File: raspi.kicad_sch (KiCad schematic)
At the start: 56 parts, among them J8 Conn_01x03, J9 debug_probe, SW1 SW_Omron_B3FS, U6 RP2350B-QFN80, U8 16Mbit PSRAM, X1 ASE-xxxMHz

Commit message: Finnished pinouts
pending input from firmware
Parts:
- added TP32, TP33, TP34: Spare, symbol Connector:TestPoint
- X1: value ASE-xxxMHz -> ASE-12.000MHZ-L-C-T
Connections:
- net BAR_CS: now also U6.26 (GPIO25)
- net Encoder0_A: now also U6.18 (GPIO18)
- net Encoder0_B: now also U6.19 (GPIO19)
- net Encoder1_A: now also U6.3 (GPIO6)
- net Encoder1_B: now also U6.4 (GPIO7)
- net Expansion_RX: now also R26.1; no longer R27.2
- net Expansion_TX: now also R27.2; no longer R26.1
- net GPS_INT: now also U6.9 (GPIO11)
- net GPS_PPS: now also U6.6 (GPIO8)
- net GPS_RESET: now also U6.7 (GPIO9)
- net GPS_RX: now also U6.1 (GPIO4)
- net GPS_SAFE: now also U6.8 (GPIO10)
- net GPS_TX: now also U6.2 (GPIO5)
- net IMU_CLK: now also U6.42 (GPIO33)
- net IMU_CS: now also U6.27 (GPIO26)
- net IMU_INT: now also U6.43 (GPIO34)
- net SD_CS: now also U6.25 (GPIO24)
- net SD_DET: now also U6.40 (GPIO32)
- net Spare_CS_0: now also U6.28 (GPIO27)
- net Spare_CS_1: now also U6.36 (GPIO28)
- net Spare_CS_2: now also U6.37 (GPIO29)
- net at U6.11 (GPIO12): now also TP32.1
- net at U6.12 (GPIO13): now also TP33.1
- net at U6.13 (GPIO14): now also TP34.1
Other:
- note added: "Note on UARTS: Prefix determines source of the TX. For example Raspi_TX indicates that the TX is coming from the Raspi"
- note added: "Resources RASPI_TX/RX | UART0 M1 | PWM1 GPS_TX/RX | UART1 M0 | PWM0 MCU_SPI | SPI0"

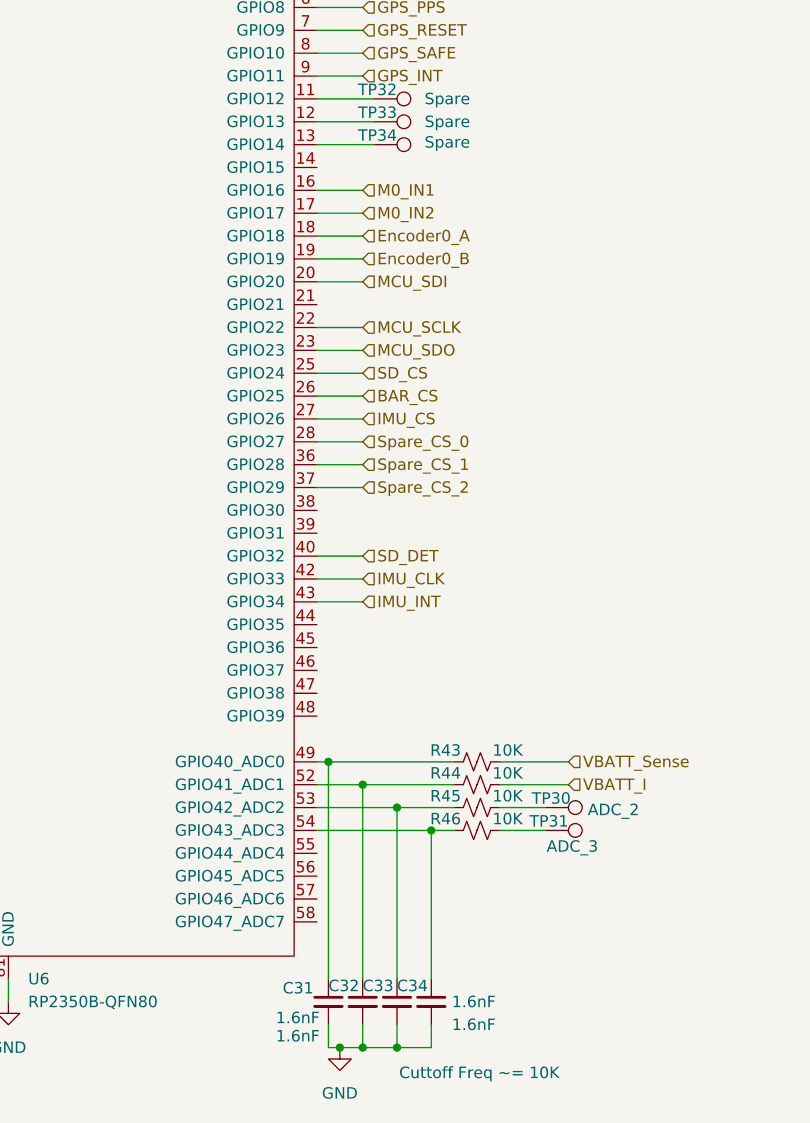
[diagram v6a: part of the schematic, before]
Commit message: Updated sheet to sheet pinout
Updated pinouts and cleared ERCs
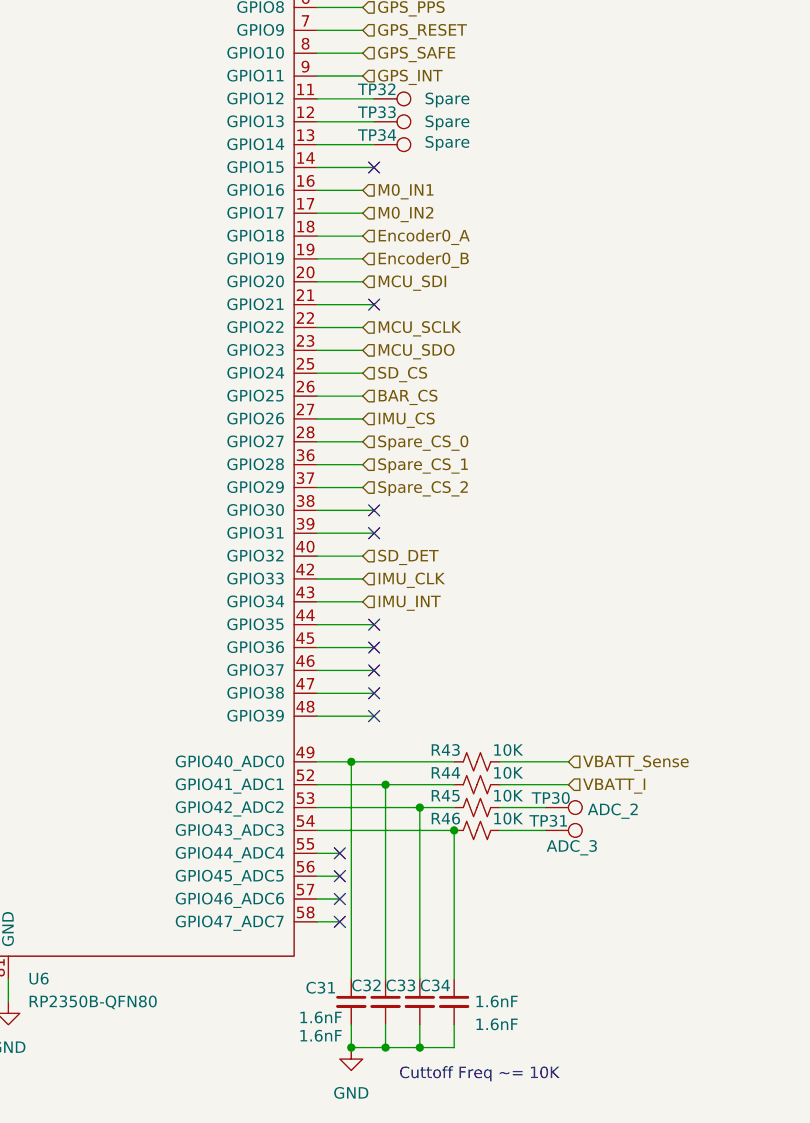
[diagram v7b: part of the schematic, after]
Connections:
- no-connect marks 1 -> 14
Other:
- moved on the sheet: C31, C32, C33, C34

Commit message: started layout
Preliminary footprint selection
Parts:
- C20, C21, C22, C27, C28, C29, C30, C31, C32, C33, C34, C35, C36, C37, C38, C39, C40, C41, C42, C43, C44: footprint (none) -> Capacitor_SMD:C_0603_1608Metric_Pad1.08x0.95mm_HandSolder
- C23, C24, C25, C26: footprint (none) -> Capacitor_SMD:C_0805_2012Metric_Pad1.18x1.45mm_HandSolder
- J8: footprint (none) -> Connector_PinHeader_2.54mm:PinHeader_1x03_P2.54mm_Vertical_SMD_Pin1Left
- J9: footprint (none) -> Connector_JST:JST_SH_SM03B-SRSS-TB_1x03-1MP_P1.00mm_Horizontal
- L2: footprint (none) -> Inductor_SMD:L_1008_2520Metric; PN (none) -> LQM2HPN3R3MG0L
- R24, R25, R26, R27, R32, R33, R34, R35, R36, R41, R43, R44, R45, R46, R47, R48, R49: footprint (none) -> Resistor_SMD:R_0603_1608Metric
- SW1: footprint (none) -> Button_Switch_SMD:SW_SPST_B3S-1000
- TP23, TP26, TP27, TP28, TP29, TP30, TP31, TP32, TP33, TP34: footprint (none) -> TestPoint:TestPoint_Pad_1.0x1.0mm
- U6: footprint (none) -> RP2350_KiCad-main:RP2350B_QFN-80_EP_10.573x10.573_Pitch0.4mm
- U8: footprint (none) -> Package_SO:SOIC-8-1EP_3.9x4.9mm_P1.27mm_EP2.29x3mm
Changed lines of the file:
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@@
 			)
 		)
-		(property "Footprint" ""
+		(property "Footprint" "Resistor_SMD:R_0603_1608Metric"
 			(at 60.96 36.83 0)
 			(effects
@@
 			)
 		)
-		(property "Footprint" ""
+		(property "Footprint" "Capacitor_SMD:C_0805_2012Metric_Pad1.18x1.45mm_HandSolder"
 			(at 64.77 58.42 0)
 			(effects
@@
 			)
 		)
-		(property "Footprint" ""
+		(property "Footprint" "Resistor_SMD:R_0603_1608Metric"
 			(at 157.48 44.45 0)
 			(effects
@@
 			)
 		)
-		(property "Footprint" ""
+		(property "Footprint" "TestPoint:TestPoint_Pad_1.0x1.0mm"
 			(at 170.18 168.91 0)
 			(effects
@@
 			)
 		)
-		(property "Footprint" ""
+		(property "Footprint" "TestPoint:TestPoint_Pad_1.0x1.0mm"
 			(at 151.13 95.25 0)
 			(effects
@@
 			)
 		)
-		(property "Footprint" ""
+		(property "Footprint" "Resistor_SMD:R_0603_1608Metric"
 			(at 30.48 148.59 0)
 			(effects
@@
 			)
 		)
-		(property "Footprint" ""
+		(property "Footprint" "Connector_PinHeader_2.54mm:PinHeader_1x03_P2.54mm_Vertical_SMD_Pin1Left"
 			(at 267.97 21.59 0)
 			(effects
@@
 			)
 		)
-		(property "Footprint" ""
+		(property "Footprint" "Connector_JST:JST_SH_SM03B-SRSS-TB_1x03-1MP_P1.00mm_Horizontal"
 			(at 20.32 146.05 0)
 			(effects
@@
 			)
 		)
-		(property "Footprint" ""
+		(property "Footprint" "TestPoint:TestPoint_Pad_1.0x1.0mm"
 			(at 170.18 171.45 0)
 			(effects
@@
 			)
 		)
-		(property "Footprint" ""
+		(property "Footprint" "Inductor_SMD:L_1008_2520Metric"
 			(at 69.85 55.88 0)
 			(effects
@@
 			)
 		)
+		(property "PN" "LQM2HPN3R3MG0L"
+			(at 69.85 55.88 90)
+			(effects
+				(font
+					(size 1.27 1.27)
+				)
+				(hide yes)
+			)
+		)
 		(pin "2"
 		)
@@
 			)
 		)
-		(property "Footprint" ""
+		(property "Footprint" "Resistor_SMD:R_0603_1608Metric"
 			(at 30.48 143.51 0)
 			(effects
@@
 			)
 		)
-		(property "Footprint" ""
+		(property "Footprint" "Capacitor_SMD:C_0603_1608Metric_Pad1.08x0.95mm_HandSolder"
 			(at 250.19 152.4 0)
 			(effects
@@
 			)
 		)
-		(property "Footprint" ""
+		(property "Footprint" "TestPoint:TestPoint_Pad_1.0x1.0mm"
 			(at 55.88 48.26 0)
 			(effects
@@
 			)
 		)
-		(property "Footprint" ""
+		(property "Footprint" "Button_Switch_SMD:SW_SPST_B3S-1000"
 			(at 264.16 142.24 0)
 			(effects
@@
 			)
 		)
-		(property "Footprint" ""
+		(property "Footprint" "Capacitor_SMD:C_0603_1608Metric_Pad1.08x0.95mm_HandSolder"
 			(at 33.02 187.96 0)
 			(effects
@@
 			)
 		)
-		(property "Footprint" ""
+		(property "Footprint" "TestPoint:TestPoint_Pad_1.0x1.0mm"
 			(at 151.13 90.17 0)
 			(effects
@@
 			)
 		)
-		(property "Footprint" ""
+		(property "Footprint" "Resistor_SMD:R_0603_1608Metric"
 			(at 162.56 163.83 0)
 			(effects
@@
 			)
 		)
-		(property "Footprint" ""
+		(property "Footprint" "Capacitor_SMD:C_0603_1608Metric_Pad1.08x0.95mm_HandSolder"
 			(at 147.32 50.8 0)
 			(effects
@@
 			)
 		)
-		(property "Footprint" ""
+		(property "Footprint" "Capacitor_SMD:C_0603_1608Metric_Pad1.08x0.95mm_HandSolder"
 			(at 26.67 187.96 0)
 			(effects
@@
 			)
 		)
-		(property "Footprint" ""
+		(property "Footprint" "Capacitor_SMD:C_0603_1608Metric_Pad1.08x0.95mm_HandSolder"
 			(at 152.4 185.42 0)
 			(effects
@@
 			)
 		)
-		(property "Footprint" ""
+		(property "Footprint" "Capacitor_SMD:C_0603_1608Metric_Pad1.08x0.95mm_HandSolder"
 			(at 54.61 187.96 0)
 			(effects
@@
 			)
 		)
-		(property "Footprint" ""
+		(property "Footprint" "Capacitor_SMD:C_0603_1608Metric_Pad1.08x0.95mm_HandSolder"
 			(at 148.59 185.42 0)
 			(effects
@@
 			)
 		)
-		(property "Footprint" ""
+		(property "Footprint" "TestPoint:TestPoint_Pad_1.0x1.0mm"
 			(at 165.1 49.53 0)
 			(effects
@@
 			)
 		)
-		(property "Footprint" ""
+		(property "Footprint" "Capacitor_SMD:C_0603_1608Metric_Pad1.08x0.95mm_HandSolder"
 			(at 69.85 187.96 0)
 			(effects
@@
 			)
 		)
-		(property "Footprint" ""
+		(property "Footprint" "Capacitor_SMD:C_0805_2012Metric_Pad1.18x1.45mm_HandSolder"
 			(at 67.31 22.86 0)
 			(effects
@@
 			)
 		)
-		(property "Footprint" ""
+		(property "Footprint" "Capacitor_SMD:C_0603_1608Metric_Pad1.08x0.95mm_HandSolder"
 			(at 39.37 187.96 0)
 			(effects
@@
 			)
 		)
-		(property "Footprint" ""
+		(property "Footprint" "Capacitor_SMD:C_0603_1608Metric_Pad1.08x0.95mm_HandSolder"
 			(at 62.23 187.96 0)
 			(effects
@@
 			)
 		)
-		(property "Footprint" ""
+		(property "Footprint" "Capacitor_SMD:C_0603_1608Metric_Pad1.08x0.95mm_HandSolder"
 			(at 46.99 187.96 0)
 			(effects
@@
 			)
 		)
-		(property "Footprint" ""
+		(property "Footprint" "Capacitor_SMD:C_0603_1608Metric_Pad1.08x0.95mm_HandSolder"
 			(at 133.35 25.4 0)
 			(effects
@@
 			)
 		)
-		(property "Footprint" ""
+		(property "Footprint" "Resistor_SMD:R_0603_1608Metric"
 			(at 21.59 101.6 0)
 			(effects
@@
 			)
 		)
-		(property "Footprint" ""
+		(property "Footprint" "Capacitor_SMD:C_0603_1608Metric_Pad1.08x0.95mm_HandSolder"
 			(at 77.47 187.96 0)
 			(effects
@@
 			)
 		)
-		(property "Footprint" ""
+		(property "Footprint" "Capacitor_SMD:C_0603_1608Metric_Pad1.08x0.95mm_HandSolder"
 			(at 74.93 22.86 0)
 			(effects
@@
 			)
 		)
-		(property "Footprint" ""
+		(property "Footprint" "Resistor_SMD:R_0603_1608Metric"
 			(at 243.84 19.05 0)
 			(effects
@@
 			)
 		)
-		(property "Footprint" ""
+		(property "Footprint" "Capacitor_SMD:C_0603_1608Metric_Pad1.08x0.95mm_HandSolder"
 			(at 156.21 185.42 0)
 			(effects
@@
 			)
 		)
-		(property "Footprint" ""
+		(property "Footprint" "Capacitor_SMD:C_0805_2012Metric_Pad1.18x1.45mm_HandSolder"
 			(at 66.04 40.64 0)
 			(effects
@@
 			)
 		)
-		(property "Footprint" ""
+		(property "Footprint" "Resistor_SMD:R_0603_1608Metric"
 			(at 162.56 161.29 0)
 			(effects
@@
 			)
 		)
-		(property "Footprint" ""
+		(property "Footprint" "Capacitor_SMD:C_0603_1608Metric_Pad1.08x0.95mm_HandSolder"
 			(at 152.4 50.8 0)
 			(effects
@@
 			)
 		)
-		(property "Footprint" ""
+		(property "Footprint" "Resistor_SMD:R_0603_1608Metric"
 			(at 139.7 21.59 0)
 			(effects
@@
 			)
 		)
-		(property "Footprint" ""
+		(property "Footprint" "TestPoint:TestPoint_Pad_1.0x1.0mm"
 			(at 165.1 52.07 0)
 			(effects
@@
 			)
 		)
-		(property "Footprint" ""
+		(property "Footprint" "Resistor_SMD:R_0603_1608Metric"
 			(at 162.56 166.37 0)
 			(effects
@@
 			)
 		)
-		(property "Footprint" ""
+		(property "Footprint" "Resistor_SMD:R_0603_1608Metric"
 			(at 243.84 21.59 0)
 			(effects
@@
 			)
 		)
-		(property "Footprint" ""
+		(property "Footprint" "Resistor_SMD:R_0603_1608Metric"
 			(at 157.48 46.99 0)
 			(effects
@@
 			)
 		)
-		(property "Footprint" ""
+		(property "Footprint" "Capacitor_SMD:C_0603_1608Metric_Pad1.08x0.95mm_HandSolder"
 			(at 20.32 187.96 0)
 			(effects
@@
 			)
 		)
-		(property "Footprint" ""
+		(property "Footprint" "Capacitor_SMD:C_0603_1608Metric_Pad1.08x0.95mm_HandSolder"
 			(at 81.28 22.86 0)
 			(effects
@@
 			)
 		)
-		(property "Footprint" ""
+		(property "Footprint" "Resistor_SMD:R_0603_1608Metric"
 			(at 250.19 143.51 0)
 			(effects
@@
 			)
 		)
-		(property "Footprint" ""
+		(property "Footprint" "RP2350_KiCad-main:RP2350B_QFN-80_EP_10.573x10.573_Pitch0.4mm"
 			(at 104.14 59.69 0)
 			(effects
@@
 			)
 		)
-		(property "Footprint" ""
+		(property "Footprint" "Package_SO:SOIC-8-1EP_3.9x4.9mm_P1.27mm_EP2.29x3mm"
 			(at 38.1 73.66 0)
 			(effects
@@
 			)
 		)
-		(property "Footprint" ""
+		(property "Footprint" "TestPoint:TestPoint_Pad_1.0x1.0mm"
 			(at 60.96 88.9 0)
 			(effects
@@
 			)
 		)
-		(property "Footprint" ""
+		(property "Footprint" "Capacitor_SMD:C_0603_1608Metric_Pad1.08x0.95mm_HandSolder"
 			(at 160.02 185.42 0)
 			(effects
@@
 			)
 		)
-		(property "Footprint" ""
+		(property "Footprint" "TestPoint:TestPoint_Pad_1.0x1.0mm"
 			(at 151.13 92.71 0)
 			(effects
@@
 			)
 		)
-		(property "Footprint" ""
+		(property "Footprint" "TestPoint:TestPoint_Pad_1.0x1.0mm"
 			(at 237.49 149.86 0)
 			(effects
@@
 			)
 		)
-		(property "Footprint" ""
+		(property "Footprint" "Resistor_SMD:R_0603_1608Metric"
 			(at 243.84 35.56 0)
 			(effects
@@
 			)
 		)
-		(property "Footprint" ""
+		(property "Footprint" "Capacitor_SMD:C_0603_1608Metric_Pad1.08x0.95mm_HandSolder"
 			(at 38.1 93.98 0)
 			(effects
@@
 			)
 		)
-		(property "Footprint" ""
+		(property "Footprint" "Capacitor_SMD:C_0603_1608Metric_Pad1.08x0.95mm_HandSolder"
 			(at 22.86 71.12 0)
 			(effects
@@
 			)
 		)
-		(property "Footprint" ""
+		(property "Footprint" "Resistor_SMD:R_0603_1608Metric"
 			(at 54.61 62.23 0)
 			(effects
@@
 			)
 		)
-		(property "Footprint" ""
+		(property "Footprint" "Resistor_SMD:R_0603_1608Metric"
 			(at 243.84 33.02 0)
 			(effects
@@
 			)
 		)
-		(property "Footprint" ""
+		(property "Footprint" "Resistor_SMD:R_0603_1608Metric"
 			(at 162.56 158.75 0)
 			(effects
@@
 			)
 		)
-		(property "Footprint" ""
+		(property "Footprint" "Capacitor_SMD:C_0805_2012Metric_Pad1.18x1.45mm_HandSolder"
 			(at 53.34 40.64 0)
 			(effects
